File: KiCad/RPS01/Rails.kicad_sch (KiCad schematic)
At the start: 58 parts, among them U1 LTC3780EG-TRPBF

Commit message: Board Ready For layout. Except for 19V Boost? CHECK vs SIM Please
Board Ready For layout. Except for 19V Boost? CHECK vs SIM Please
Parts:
- removed QA(1)_19V_2, QB(2)_19V_1, QC(4)_19V_1, QD(3)_19V_3: BSC009NE2LS5IATMA1, Mechatronic Footprints:PG-TDSON-8_INF_modified_ken, symbol Mechatronics NMOS:BSC009NE2LS5IATMA1
- added F2: 3, Mechatronics Fuses:0154Series_LTF, symbol Device:Fuse_Small
- added F3: 15, Mechatronics Fuses:0154Series_LTF, symbol Device:Fuse_Small
- added Q_A1, Q_B1, Q_C1, Q_D1: BSC009NE2LS5IATMA1, Mechatronics MOSFET:PG-TDSON-8_INF, symbol Mechatronics 19V MOSFET:BSC009NE2LS5IATMA1
- added R8, R9: 0, Resistor_SMD:R_0603_1608Metric, symbol Device:R_Small
- C_ESR1: renamed from C(lowESR)1; footprint Mechatronics Cesr:CAPMP7.6X4.3_3.1N_KEM -> Mechatronic Footprints:LOWESRCAPMP7.6X4.3_3.1N_KEM
- C_FF?: value 3.3nF -> 3.3n
- C_FF?: value 10.75nF -> 10.75n
- C_P3: renamed from Cout_19V_EEH-ZU1V331P1; symbol Device:C -> Device:C_Polarized_Small
- C_P5: renamed from Cin(b)1; symbol Device:C -> Device:C_Polarized_Small
- D_S2: renamed from D5_19V1; value D_Schottky_B340AE-13 -> B340AE-13
- D_S4: renamed from D4_19V1; value D_Schottky_B340AE-13 -> B340AE-13
- D_Z1: renamed from D(Zener)_19V1; value D_Zener_BZT52C4V7-13-F -> BZT52C4V7-13-F
- F1: value 2A -> 2
- F4: renamed from F2; value 5A -> 5
- F5: renamed from F3; value 5A -> 5
- R? (x4): footprint Resistor_SMD:R_1206_3216Metric -> Resistor_SMD:R_0603_1608Metric
- renumbered Ca(SW1)1 to C10, Cs1 to C11, Css1 to C12, Cth1 to C13, Cthp1 to C14, Cb(SW2)1 to C16, Cc(out)1 to C17, C(STBYMD)1 to C18, Cin(c)1 to C19, Cout_b_19V_EEH-ZU1V331P1 to C_P4, D2(1)_19V1 to D_S1, D1(2)_19V1 to D_S3, L1_19V1 to L1, R13 to R10, R4 to R11, R(pgood)1 to R12, R5 to R13, Rth1 to R14, Rin(Run)1 to R15, R14 to R16, R8 to R7, Rt1 to R_P3, Rb1 to R_P4, Rsen1 to R_S2, Rs1 to R_S3, U1 to U15
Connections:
- net Vin is gone; now on net +BATT: C19.1, C_P5.1, R15.1, U15.21 (VIN)
- net +19V: now also C17.1, C_P3.1, C_P4.1, R_P3.1, F3.2, R9.2
- net +BATT: now also Q_A1.5, Q_A1.6, Q_A1.7, Q_A1.8
- net BG1: now also Q_C1.4
- net BG2: now also Q_B1.4
- net LOGIC 5V: now also F2.2, R8.2; no longer U?.2 (VO), U?.2 (VO)
- net Rsense: now also Q_B1.1, Q_B1.2, Q_B1.3, Q_C1.1, Q_C1.2, Q_C1.3
- net SW1: now also Q_C1.5, Q_C1.6, Q_C1.7, Q_C1.8, Q_D1.1, Q_D1.2, Q_D1.3
- net SW2: now also Q_A1.1, Q_A1.2, Q_A1.3, Q_B1.5, Q_B1.6, Q_B1.7, Q_B1.8
- net TG1: now also Q_D1.4
- net TG2: now also Q_A1.4
- removed net Vout: C17.1, C_P3.1, C_P4.1, D_S1.1, R_P3.1
- new net: F2.1, R8.1, U?.2 (VO), U?.2 (VO)
- new net: D_S1.1, F3.1, Q_D1.5, Q_D1.6, Q_D1.7, Q_D1.8, R9.1
- no-connect marks 3 -> 1
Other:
- note removed: "Forward feedback"
- moved on the sheet: C10, C11, C12, C13, C14, C16, C17, C18, C19, C_ESR1, C_FF?, C_IN?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

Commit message: Updates
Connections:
- net LOGIC 5V OUT: now reaches F2.1, R8.1, U?.2 (VO), U?.2 (VO)
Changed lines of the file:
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@@
     (effects (font (size 1 1)) (justify left bottom))
+  )
+  (label "LOGIC 5V OUT" (at 95.504 80.518 0) (fields_autoplaced)
+    (effects (font (size 1.27 1.27)) (justify left bottom))
   )
   (label "Run" (at 256.54 181.102 0) (fields_autoplaced)

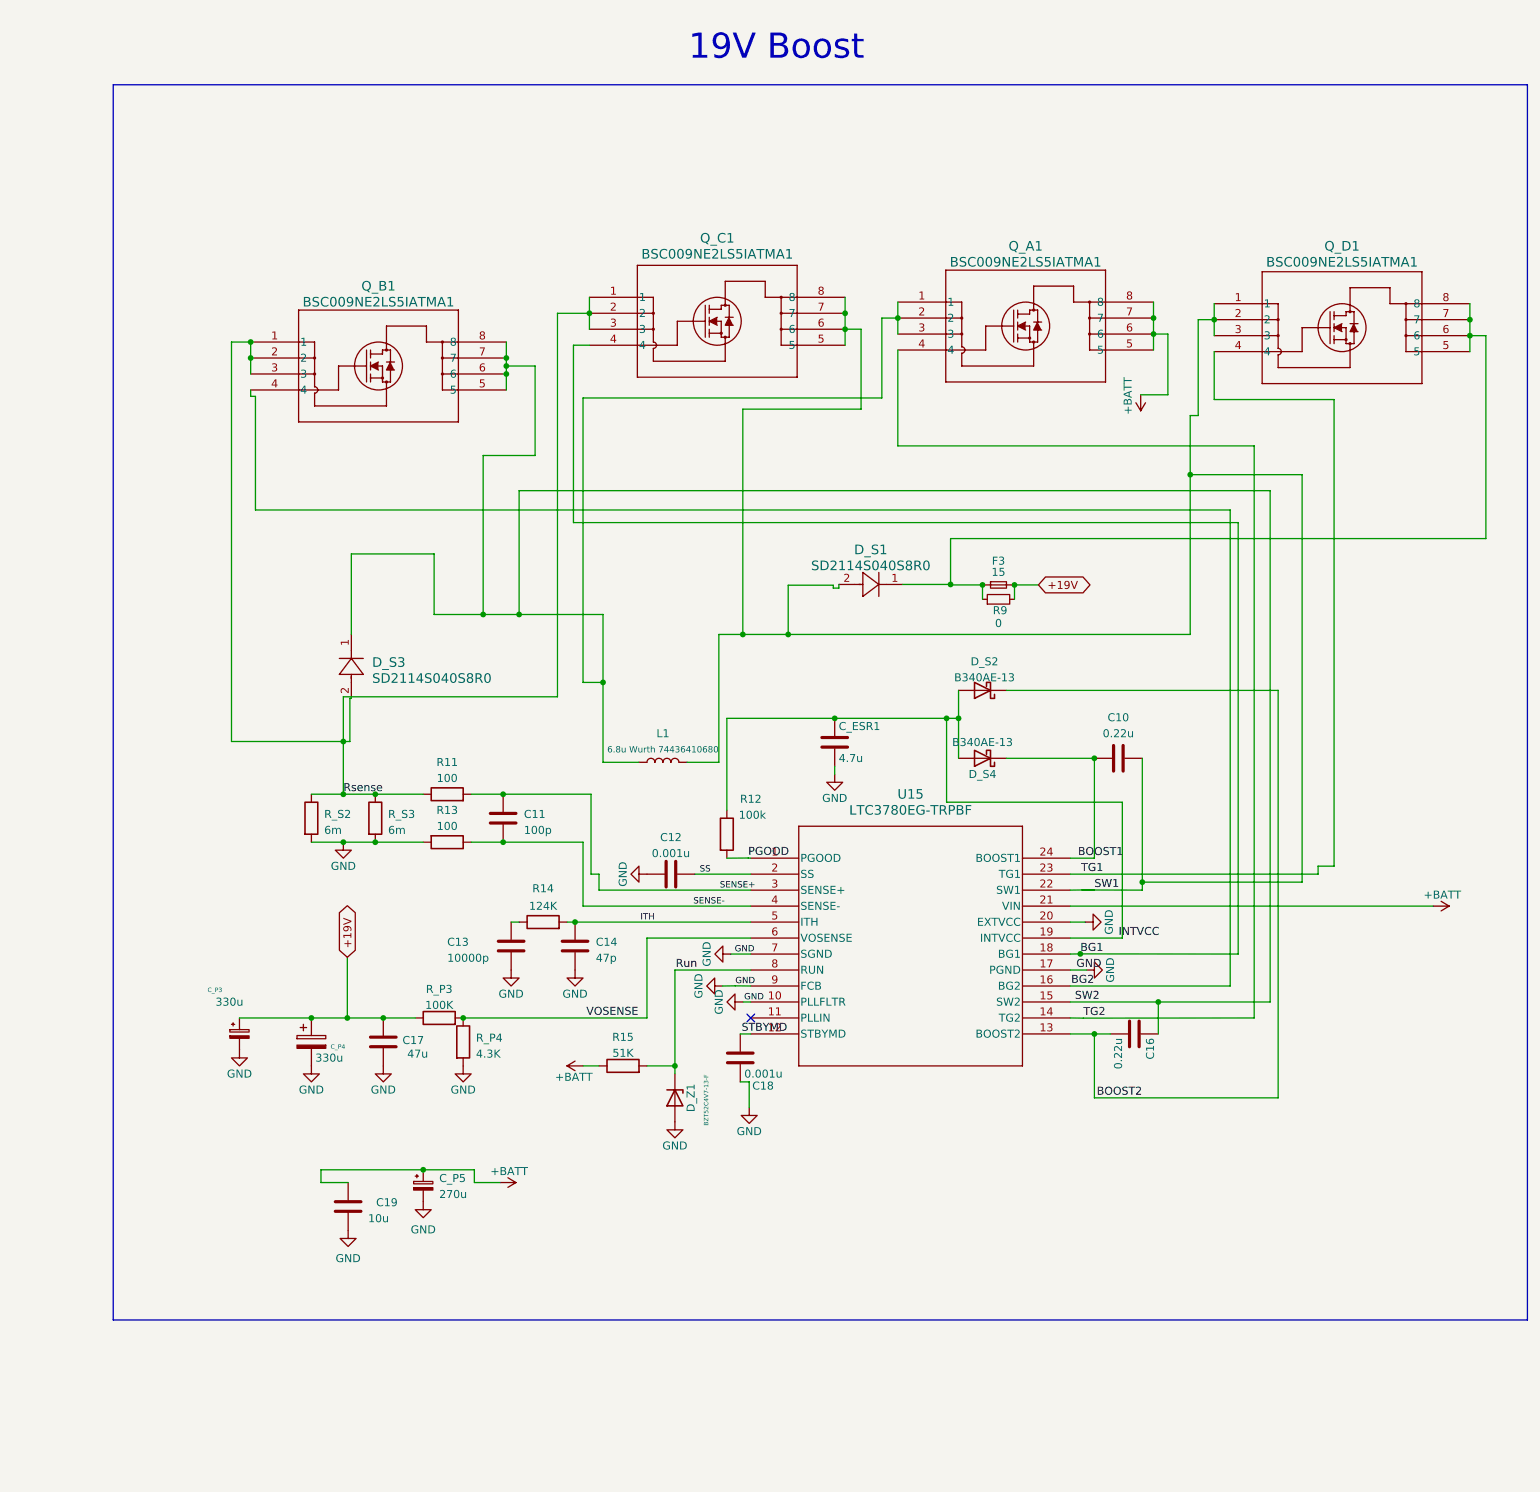
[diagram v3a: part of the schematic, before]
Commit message: changed ltc3780 to the small one
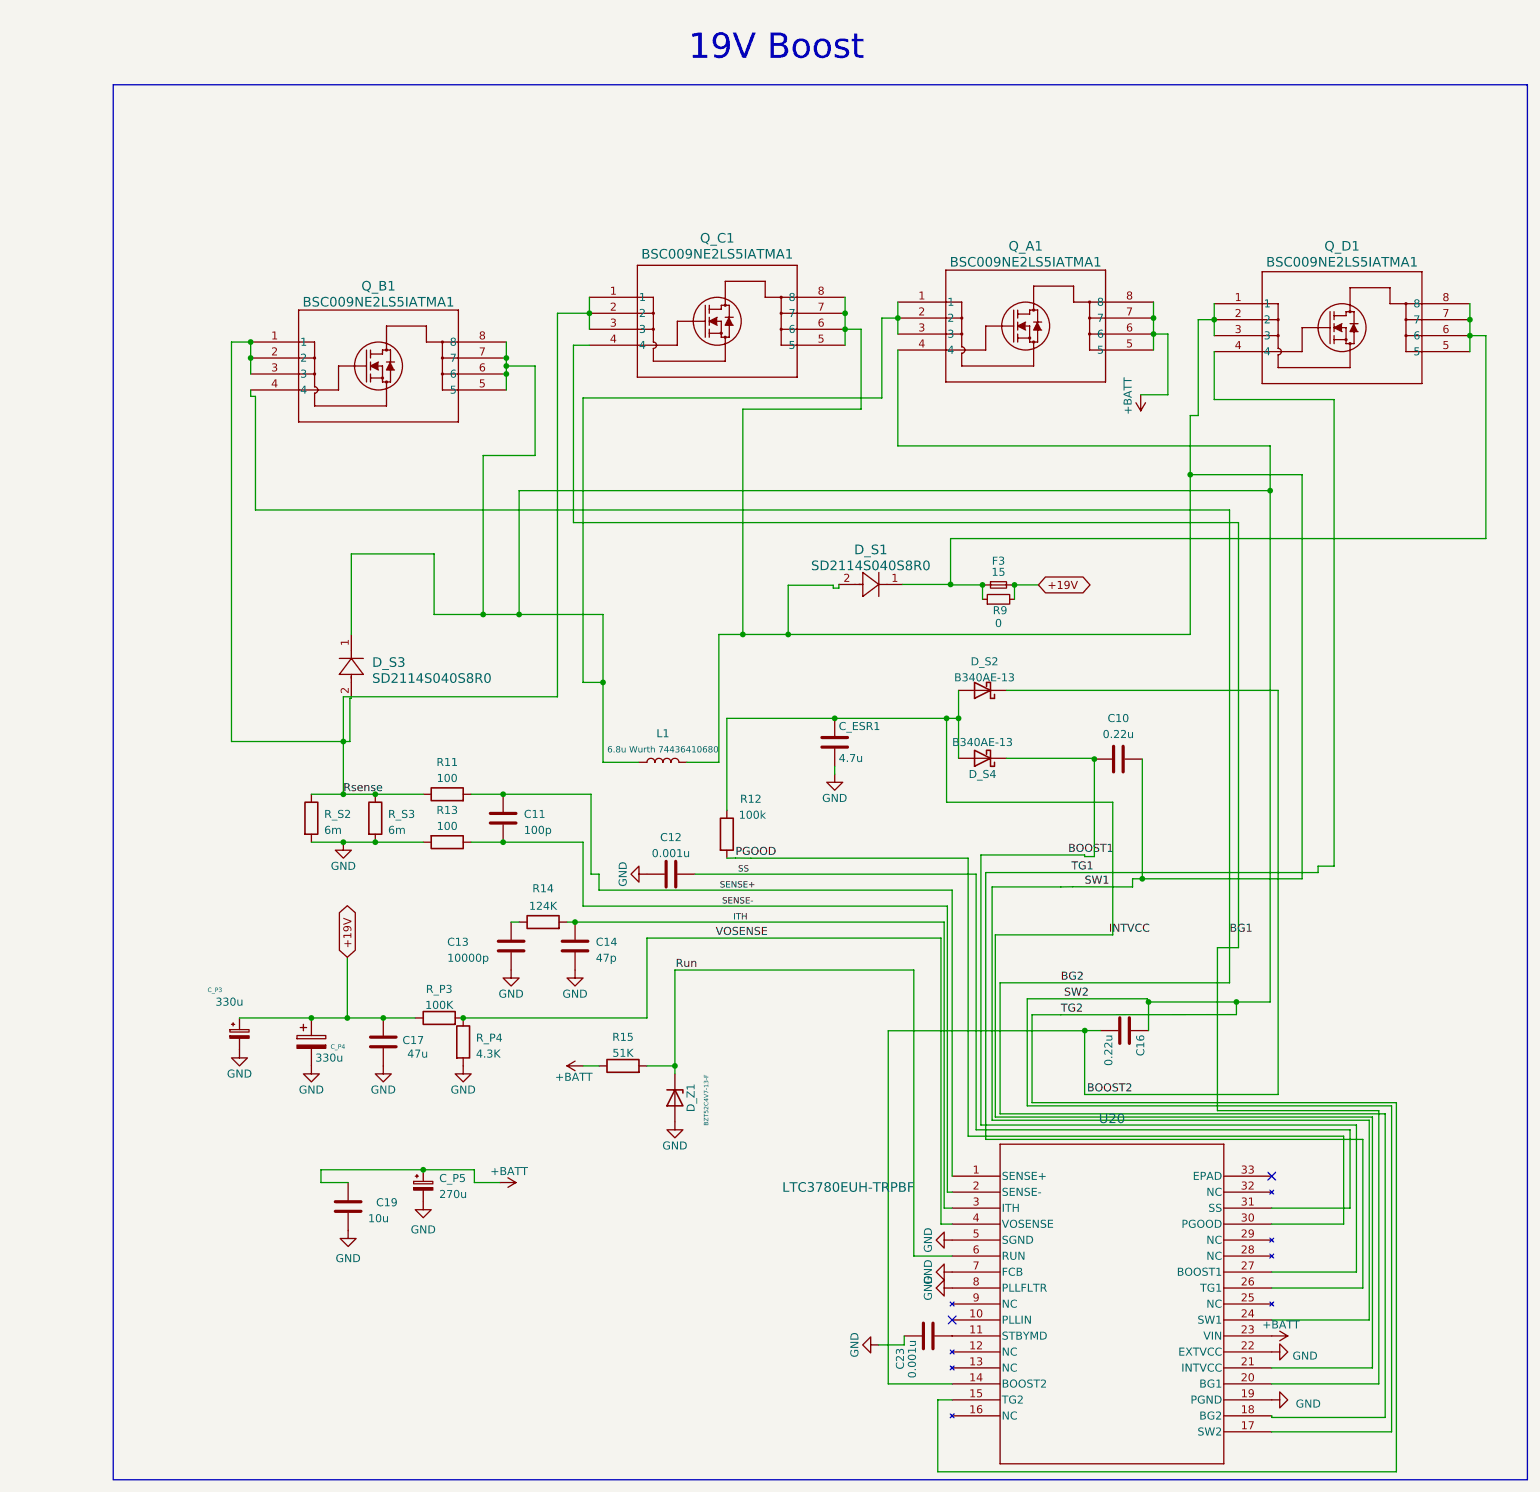
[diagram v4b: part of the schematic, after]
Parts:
- removed C18: 0.001u, Capacitor_SMD:C_1206_3216Metric, symbol Device:C
- removed U15: LTC3780EG-TRPBF, Mechatronic Footprints:LTC3780_SSOP-24_G_LIT, symbol LTC3780-24-SSOP:LTC3780EG-TRPBF
- added C23: 0.001u, Capacitor_SMD:C_1206_3216Metric, symbol Device:C
- added U20: LTC3780EUH-TRPBF, Mechatronic Footprints:QFN-32_UH_LIT, symbol Mechatronics LTC3780 Small:LTC3780EUH-TRPBF
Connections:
- net BG2 is gone; now on net BG1: Q_B1.4
- net TG2 is gone; now on net SW2: Q_A1.4
- net +BATT: now also U20.23 (VIN)
- net BG1: now also U20.18 (BG2); no longer Q_C1.4
- net BOOST1: now also U20.27 (BOOST1)
- net BOOST2: now also U20.14 (BOOST2)
- net GND: now also C23.2, U20.19 (PGND), U20.22 (EXTVCC), U20.5 (SGND), U20.7 (FCB), U20.8 (PLLFLTR)
- net INTVCC: now also U20.21 (INTVCC)
- net ITH: now also U20.3 (ITH)
- net PGOOD: now also U20.30 (PGOOD)
- net Run: now also U20.6 (RUN)
- net SENSE+: now also U20.1 (SENSE+)
- net SENSE-: now also U20.2 (SENSE-)
- net SS: now also U20.31 (SS)
- net SW1: now also U20.24 (SW1)
- net SW2: now also U20.15 (TG2), U20.17 (SW2)
- net TG1: now also U20.26 (TG1)
- net VOSENSE: now also U20.4 (VOSENSE)
- new net: Q_C1.4, U20.20 (BG1)
- new net: C23.1, U20.11 (STBYMD)
- no-connect marks 1 -> 2
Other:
- moved on the sheet: C16

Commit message: add jason signature and fix resistor footprint
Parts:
- R12: footprint LED_SMD:LED_1206_3216Metric -> Resistor_SMD:R_1206_3216Metric
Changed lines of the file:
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@@
       (effects (font (size 1.27 1.27)))
     )
-    (property "Footprint" "LED_SMD:LED_1206_3216Metric" (at 262.89 159.512 90)
+    (property "Footprint" "Resistor_SMD:R_1206_3216Metric" (at 262.89 159.512 90)
       (effects (font (size 1.27 1.27)) hide)
     )

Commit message: update cap and resistor values
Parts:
- F3: value 15 -> 10
- R?: value 9.75k -> 9.76k
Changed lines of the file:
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@@
       (effects (font (size 1.27 1.27)))
     )
-    (property "Value" "15" (at 307.848 117.856 0)
+    (property "Value" "10" (at 307.848 117.856 0)
       (effects (font (size 1.27 1.27)))
     )
@@
       (effects (font (size 1.27 1.27)) (justify right))
     )
-    (property "Value" "9.75k" (at 103.886 189.484 90)
+    (property "Value" "9.76k" (at 103.886 189.484 90)
       (effects (font (size 1.27 1.27)) (justify right))
     )

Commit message: Updated Caps
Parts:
- C_P3, C_P4: footprint Mechatronic Footprints:LargeCAPSCAPPRD350W60D800H1200 -> Mechatronics Cap:CAP_EEHZU1V331P
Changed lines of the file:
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@@
       (effects (font (size 1.27 1.27)) (justify left))
     )
-    (property "Footprint" "Mechatronic Footprints:LargeCAPSCAPPRD350W60D800H1200" (at 187.198 191.262 0)
+    (property "Footprint" "Mechatronics Cap:CAP_EEHZU1V331P" (at 187.198 191.262 0)
       (effects (font (size 1.27 1.27)) hide)
     )
@@
       (effects (font (size 1.27 1.27)) (justify left))
     )
-    (property "Footprint" "Mechatronic Footprints:LargeCAPSCAPPRD350W60D800H1200" (at 199.5932 196.342 0)
-      (effects (font (size 1.27 1.27)) hide)
-    )
+    (property "Footprint" "Mechatronics Cap:CAP_EEHZU1V331P" (at 199.5932 196.342 0)
+      (effects (font (size 1.27 1.27)) hide)
+    )

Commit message: Push
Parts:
- added R34, R35, R36, R37, R38, R39: 603_LED, Resistor_SMD:R_0603_1608Metric, symbol Device:R_Small
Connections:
- net +12V: now also R34.1
- net +19V: now also R37.1
- net +5V: now also R35.1
- net GND: now also R36.2, R38.2, R39.2
- net PD2: now reaches F1.2, R7.2, U?.2 (VO)
- new net ADC6: R37.2, R38.1
- new net ADC7: R35.2, R36.1
- new net PB0: R34.2, R39.1
